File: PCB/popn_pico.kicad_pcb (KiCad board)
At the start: 2 copper layers, 180 x 85 mm, 39 parts, among them SW1 KAN4542-0701C, SW2 KAN4542-0701C, U1 Pico

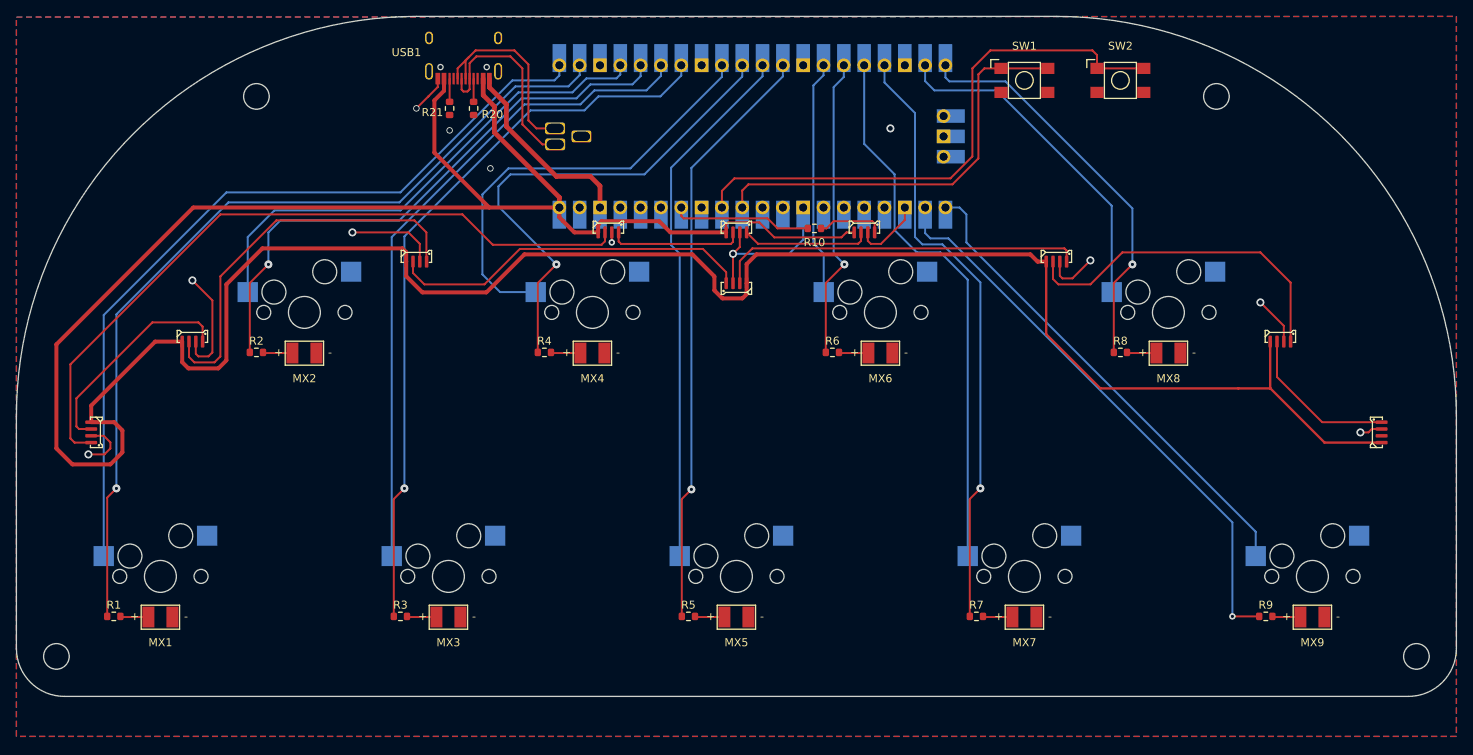
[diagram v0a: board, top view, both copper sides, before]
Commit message: Fixed PCB bug (LED 5v and GND swapped)
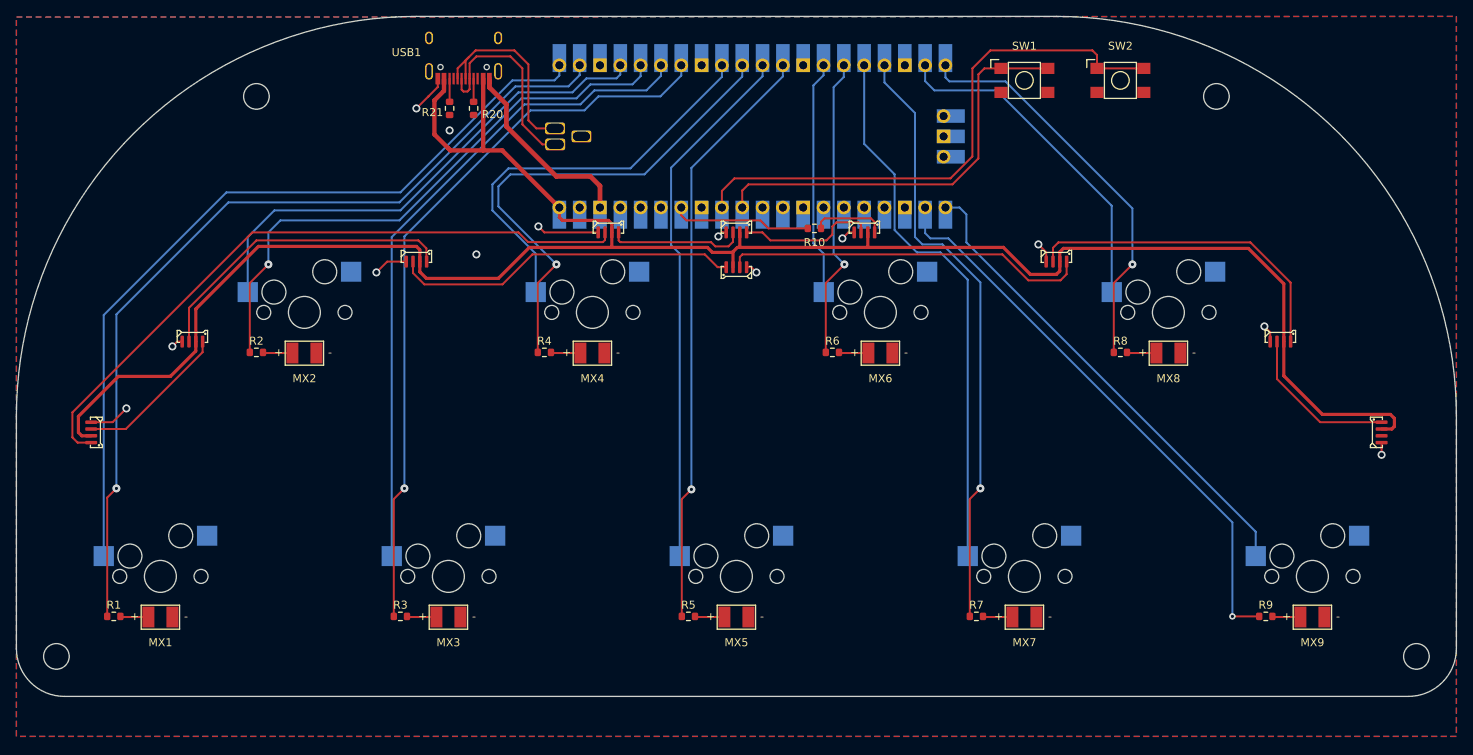
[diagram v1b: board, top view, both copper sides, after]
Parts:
- moved LED7 2.00 mm to (147.3, 94.4)
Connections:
- LED1 pad 2: GND -> +5V
- LED1 pad 4: +5V -> GND
- LED10 pad 2: GND -> +5V
- LED10 pad 4: +5V -> GND
- LED2 pad 2: GND -> +5V
- LED2 pad 4: +5V -> GND
- LED3 pad 2: GND -> +5V
- LED3 pad 4: +5V -> GND
- LED4 pad 2: GND -> +5V
- LED4 pad 4: +5V -> GND
- LED5 pad 2: GND -> +5V
- LED5 pad 4: +5V -> GND
- LED6 pad 2: GND -> +5V
- LED6 pad 4: +5V -> GND
- LED7 pad 2: GND -> +5V
- LED7 pad 4: +5V -> GND
- LED8 pad 2: GND -> +5V
- LED8 pad 4: +5V -> GND
- LED9 pad 2: GND -> +5V
- LED9 pad 4: +5V -> GND
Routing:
- net +5V: track 398.0 -> 260.5 mm
- net GND: track 106.6 -> 58.5 mm, vias 12 -> 13
- net Net-(LED5-Pad3): track 49.4 -> 39.5 mm
- net Net-(LED4-Pad3): track 27.3 -> 19.2 mm
- net Net-(LED3-Pad3): track 89.5 -> 83.2 mm
- net Net-(MX4-Pad1): track 55.1 -> 51.4 mm
- net Net-(LED6-Pad3): track 45.6 -> 43.4 mm
- net Net-(LED8-Pad3): track 42.8 -> 41.2 mm
- net Net-(LED1-Pad3): track 16.1 -> 17.3 mm
- net Net-(LED1-Pad1): track 8.31 -> 9.19 mm

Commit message: LED9 pin changed to support PWM, UF2 firmware updated too
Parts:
- removed REF** (x4): MountingHole_3.2mm_M3, MountingHole:MountingHole_3.2mm_M3
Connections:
- R9 pad 1: Net-(R9-Pad1) -> Net-(U1-Pad24)
- U1 pad 22: Net-(R9-Pad1) -> unconnected-(U1-Pad22)
- U1 pad 24: unconnected-(U1-Pad24) -> Net-(U1-Pad24)
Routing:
- net Net-(U1-Pad24): track 0.00 -> 76.7 mm, vias 0 -> 1
- net Net-(R9-Pad1): track 71.7 -> 0.00 mm, vias 1 -> 0
- net Net-(MX7-Pad1): track 68.4 -> 73.5 mm
- net Net-(R7-Pad1): track 75.9 -> 79.9 mm

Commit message: Fixed missing screw holes
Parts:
- added REF**: MountingHole_3.2mm_M3, MountingHole:MountingHole_3.2mm_M3, F.Cu at (207.3, 72.4)
- added REF**: MountingHole_3.2mm_M3, MountingHole:MountingHole_3.2mm_M3, F.Cu at (232.3, 142.4)
- added REF**: MountingHole_3.2mm_M3, MountingHole:MountingHole_3.2mm_M3, F.Cu at (62.3, 142.4)
- added REF**: MountingHole_3.2mm_M3, MountingHole:MountingHole_3.2mm_M3, F.Cu at (87.3, 72.4)
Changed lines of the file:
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@@
     )
+  )
+  (footprint "MountingHole:MountingHole_3.2mm_M3" locked (layer "F.Cu")
+    (at 207.32 72.4)
+    (descr "Mounting Hole 3.2mm, no annular, M3")
+    (tags "mounting hole 3.2mm no annular m3")
+    (attr exclude_from_pos_files exclude_from_bom)
+    (fp_text reference "REF**" (at 0 -4.2) (layer "F.SilkS") hide
+      (effects (font (size 1 1) (thickness 0.15)))
+    )
+    (fp_text value "MountingHole_3.2mm_M3" (at 0 4.2) (layer "F.Fab")
+      (effects (font (size 1 1) (thickness 0.15)))
+    )
+    (fp_text user "${REFERENCE}" (at -2 -4.5) (layer "F.Fab") hide
+      (effects (font (size 1 1) (thickness 0.15)))
+    )
+    (fp_circle (center 0 0) (end 3.2 0) (layer "Cmts.User") (width 0.15) (fill none))
+    (fp_circle (center 0 0) (end 3.45 0) (layer "F.CrtYd") (width 0.05) (fill none))
+    (pad "" np_thru_hole circle locked (at 0 0) (size 3.2 3.2) (drill 3.2) (layers *.Cu *.Mask))
   )
   (footprint "Resistor_SMD:R_0603_1608Metric" (layer "F.Cu")
@@
     )
   )
+  (footprint "MountingHole:MountingHole_3.2mm_M3" locked (layer "F.Cu")
+    (at 232.32 142.4)
+    (descr "Mounting Hole 3.2mm, no annular, M3")
+    (tags "mounting hole 3.2mm no annular m3")
+    (attr exclude_from_pos_files exclude_from_bom)
+    (fp_text reference "REF**" (at 0 -4.2) (layer "F.SilkS") hide
+      (effects (font (size 1 1) (thickness 0.15)))
+    )
+    (fp_text value "MountingHole_3.2mm_M3" (at 0 4.2) (layer "F.Fab")
+      (effects (font (size 1 1) (thickness 0.15)))
+    )
+    (fp_text user "${REFERENCE}" (at 0 0) (layer "F.Fab") hide
+      (effects (font (size 1 1) (thickness 0.15)))
+    )
+    (fp_circle (center 0 0) (end 3.2 0) (layer "Cmts.User") (width 0.15) (fill none))
+    (fp_circle (center 0 0) (end 3.45 0) (layer "F.CrtYd") (width 0.05) (fill none))
+    (pad "" np_thru_hole circle locked (at 0 0) (size 3.2 3.2) (drill 3.2) (layers *.Cu *.Mask))
+  )
   (footprint "Resistor_SMD:R_0603_1608Metric" (layer "F.Cu")
     (at 159.32 104.4)
@@
     )
   )
+  (footprint "MountingHole:MountingHole_3.2mm_M3" locked (layer "F.Cu")
+    (at 62.32 142.4)
+    (descr "Mounting Hole 3.2mm, no annular, M3")
+    (tags "mounting hole 3.2mm no annular m3")
+    (attr exclude_from_pos_files exclude_from_bom)
+    (fp_text reference "REF**" (at 0 -4.2) (layer "F.SilkS") hide
+      (effects (font (size 1 1) (thickness 0.15)))
+    )
+    (fp_text value "MountingHole_3.2mm_M3" (at 0 4.2) (layer "F.Fab")
+      (effects (font (size 1 1) (thickness 0.15)))
+    )
+    (fp_text user "${REFERENCE}" (at 0 0) (layer "F.Fab") hide
+      (effects (font (size 1 1) (thickness 0.15)))
+    )
+    (fp_circle (center 0 0) (end 3.2 0) (layer "Cmts.User") (width 0.15) (fill none))
+    (fp_circle (center 0 0) (end 3.45 0) (layer "F.CrtYd") (width 0.05) (fill none))
+    (pad "" np_thru_hole circle locked (at 0 0) (size 3.2 3.2) (drill 3.2) (layers *.Cu *.Mask))
+  )
   (footprint "MX_Only:MXOnly-Popn_Button-Hotswap-LED" (layer "F.Cu")
     (at 93.32 99.4)
@@
     )
   )
+  (footprint "MountingHole:MountingHole_3.2mm_M3" locked (layer "F.Cu")
+    (at 87.32 72.4)
+    (descr "Mounting Hole 3.2mm, no annular, M3")
+    (tags "mounting hole 3.2mm no annular m3")
+    (attr exclude_from_pos_files exclude_from_bom)
+    (fp_text reference "REF**" (at 0 -4.2) (layer "F.SilkS") hide
+      (effects (font (size 1 1) (thickness 0.15)))
+    )
+    (fp_text value "MountingHole_3.2mm_M3" (at 0 4.2) (layer "F.Fab")
+      (effects (font (size 1 1) (thickness 0.15)))
+    )
+    (fp_text user "${REFERENCE}" (at 0 0) (layer "F.Fab") hide
+      (effects (font (size 1 1) (thickness 0.15)))
+    )
+    (fp_circle (center 0 0) (end 3.2 0) (layer "Cmts.User") (width 0.15) (fill none))
+    (fp_circle (center 0 0) (end 3.45 0) (layer "F.CrtYd") (width 0.05) (fill none))
+    (pad "" np_thru_hole circle locked (at 0 0) (size 3.2 3.2) (drill 3.2) (layers *.Cu *.Mask))
+  )
   (footprint "agg:WS2812B-4020" (layer "F.Cu")
